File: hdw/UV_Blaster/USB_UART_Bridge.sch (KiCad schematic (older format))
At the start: 28 parts

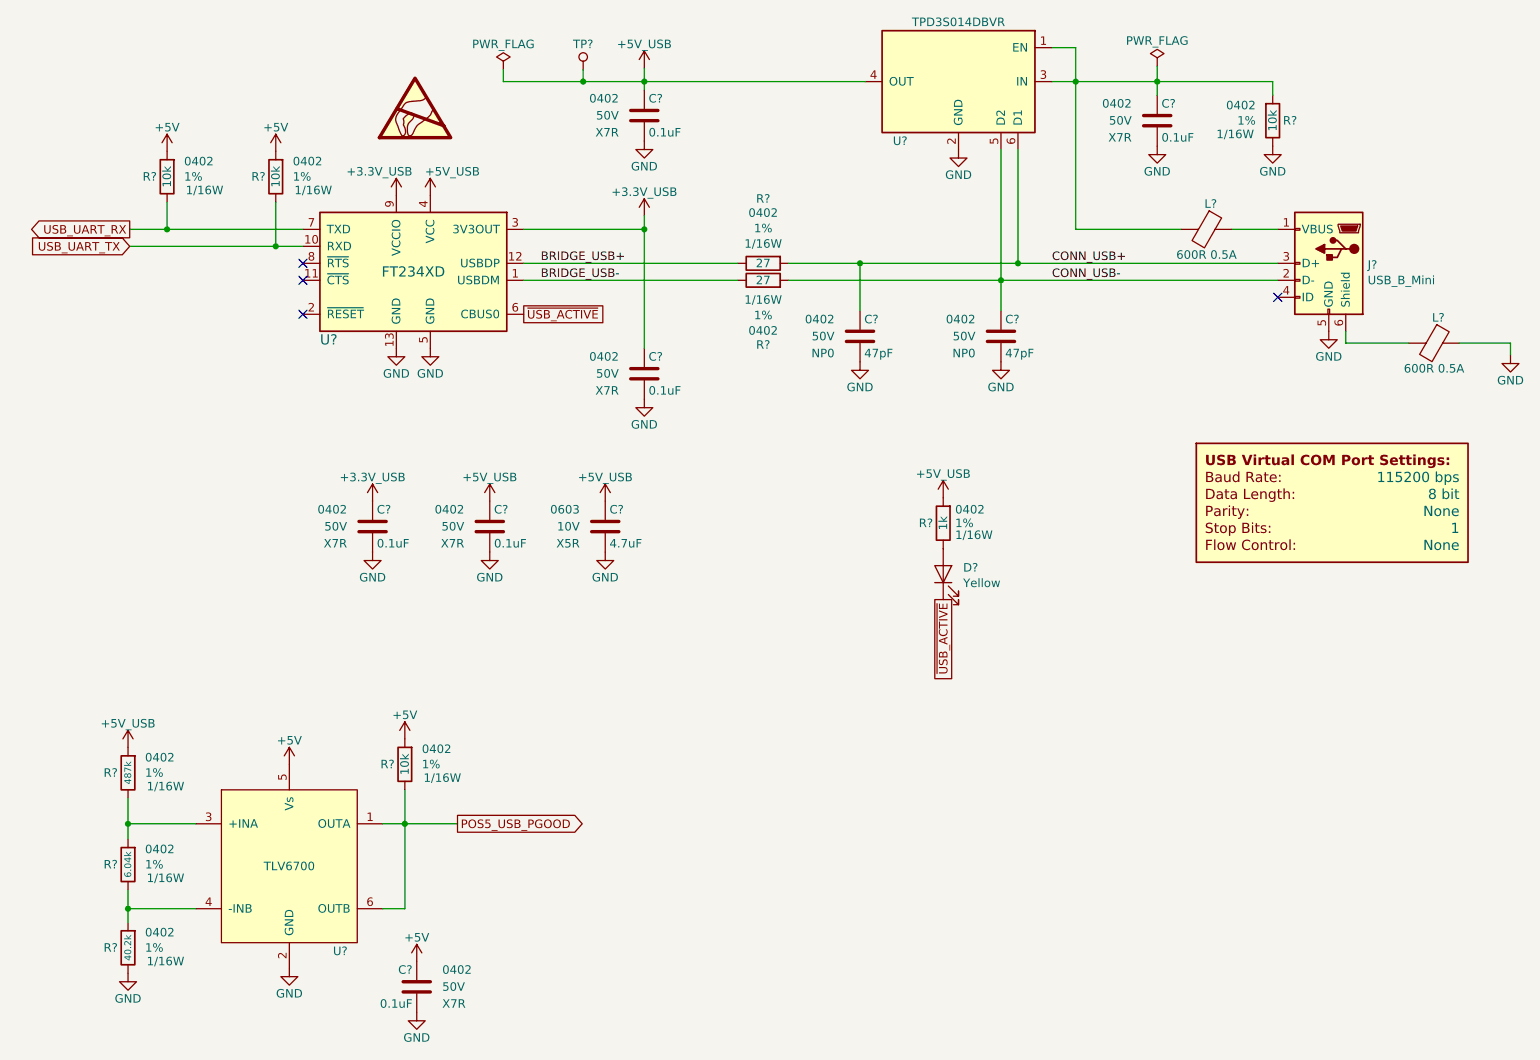
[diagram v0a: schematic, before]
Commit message: More sch work, netlist, part numbers, footprints
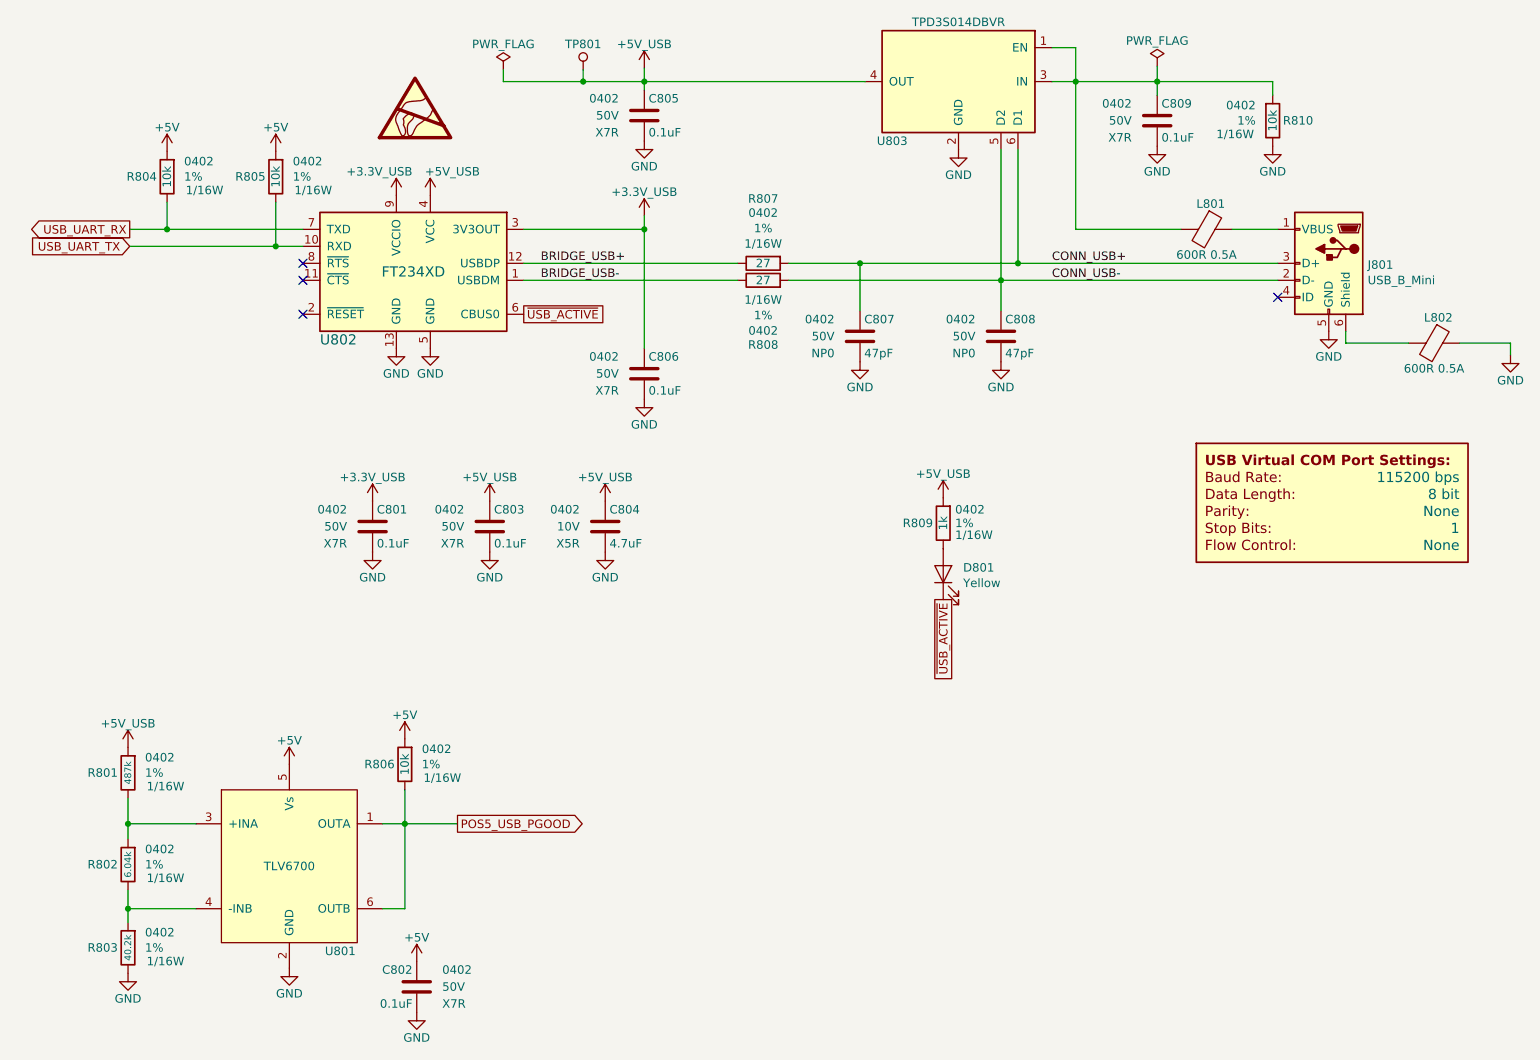
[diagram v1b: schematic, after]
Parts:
- C804: renamed from C?; footprint Capacitors_SMD:C_0603 -> Capacitors_SMD:C_0402; Digi-Key PN 490-16348-1-ND -> 490-14306-1-ND; display_footprint 0603 -> 0402
- C807, C808: renamed from C?; footprint (none) -> Capacitors_SMD:C_0402; Digi-Key PN (none) -> 399-7796-1-ND
- D801: renamed from D?; footprint (none) -> LEDs:LED_0402; Digi-Key PN (none) -> 754-1809-1-ND
- L801, L802: renamed from L?; footprint Inductors_SMD:L_0603 -> Inductors_SMD:L_0402; Digi-Key PN 732-2389-1-ND -> 490-16584-1-ND
- R801: renamed from R?; Digi-Key PN (none) -> YAG2372CT-ND
- R802: renamed from R?; Digi-Key PN (none) -> RMCF0402FT6K04CT-ND
- R803: renamed from R?; Digi-Key PN (none) -> P40.2KLCT-ND
- R804, R805, R806, R810: renamed from R?; Digi-Key PN RMCF0402FT10K0CT-ND -> 541-3959-1-ND
- R807, R808: renamed from R?; Digi-Key PN (none) -> P27.0LCT-ND
- R809: renamed from R?; Digi-Key PN 541-1.00KLCT-ND -> P1.00KLCT-ND
- gave numbers to parts that had none: 12
